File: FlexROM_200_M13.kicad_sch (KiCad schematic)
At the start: 9 parts, among them J1 HN61364_TANDY_200_M13, U1 FM16W08, U2 74LVC2G00

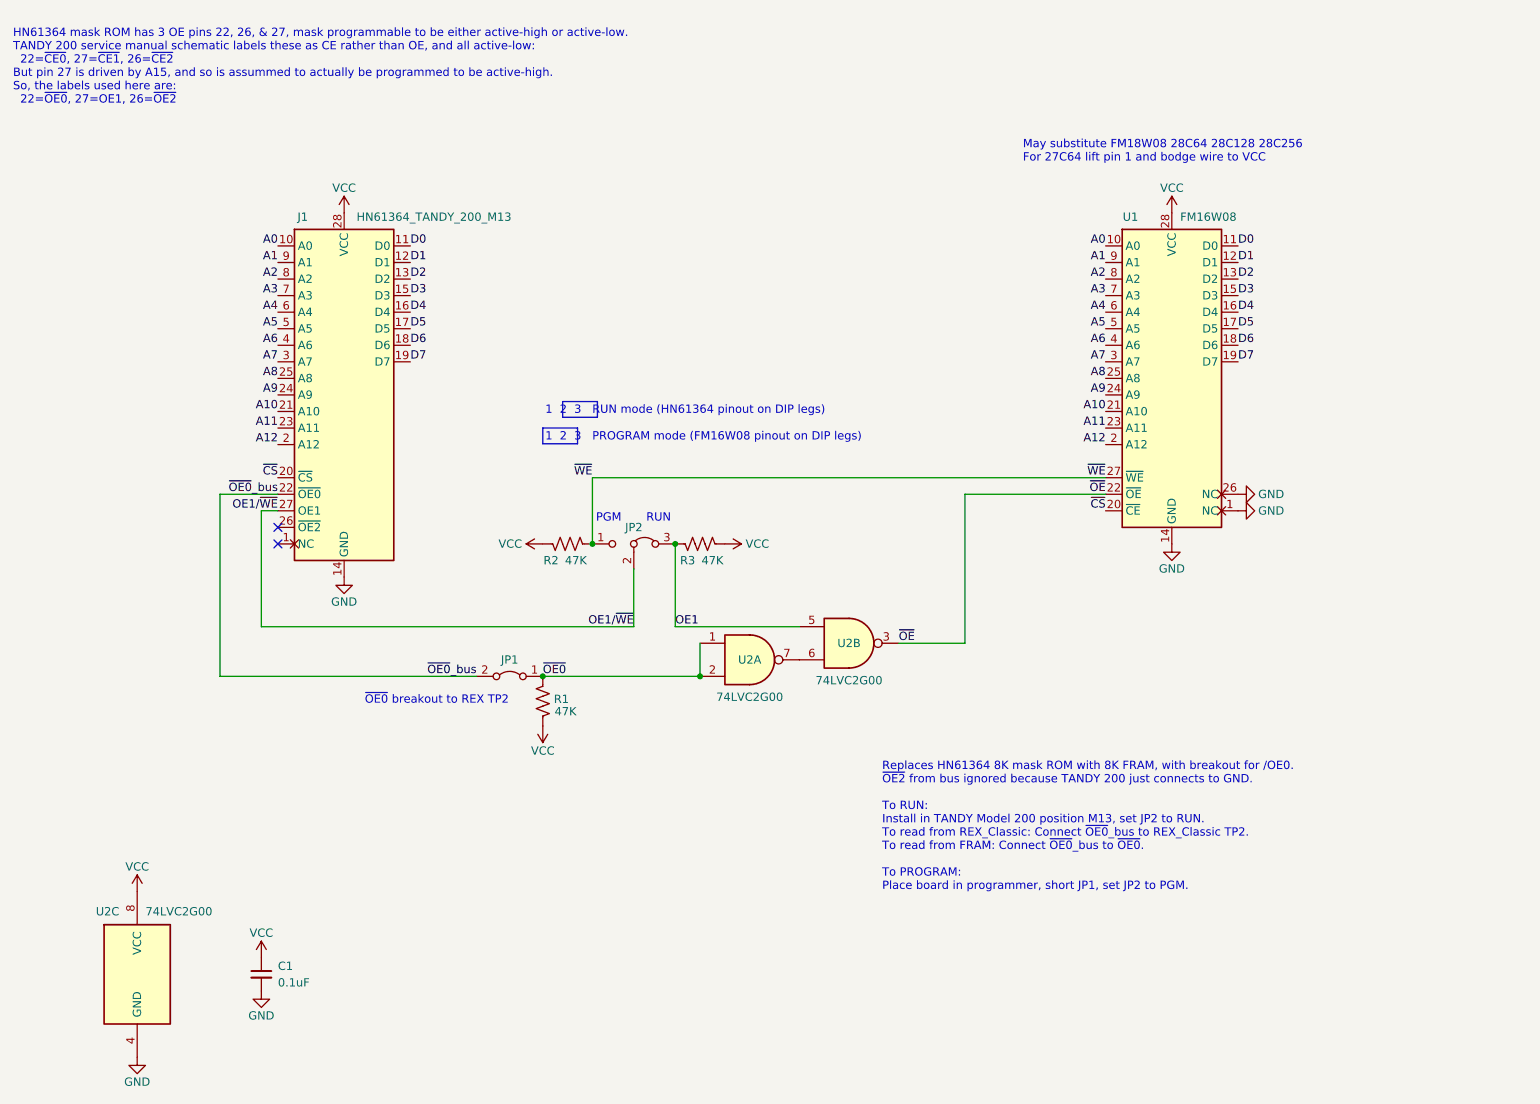
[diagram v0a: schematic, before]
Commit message: flexrom 102 & 200 accept eeprom or fram
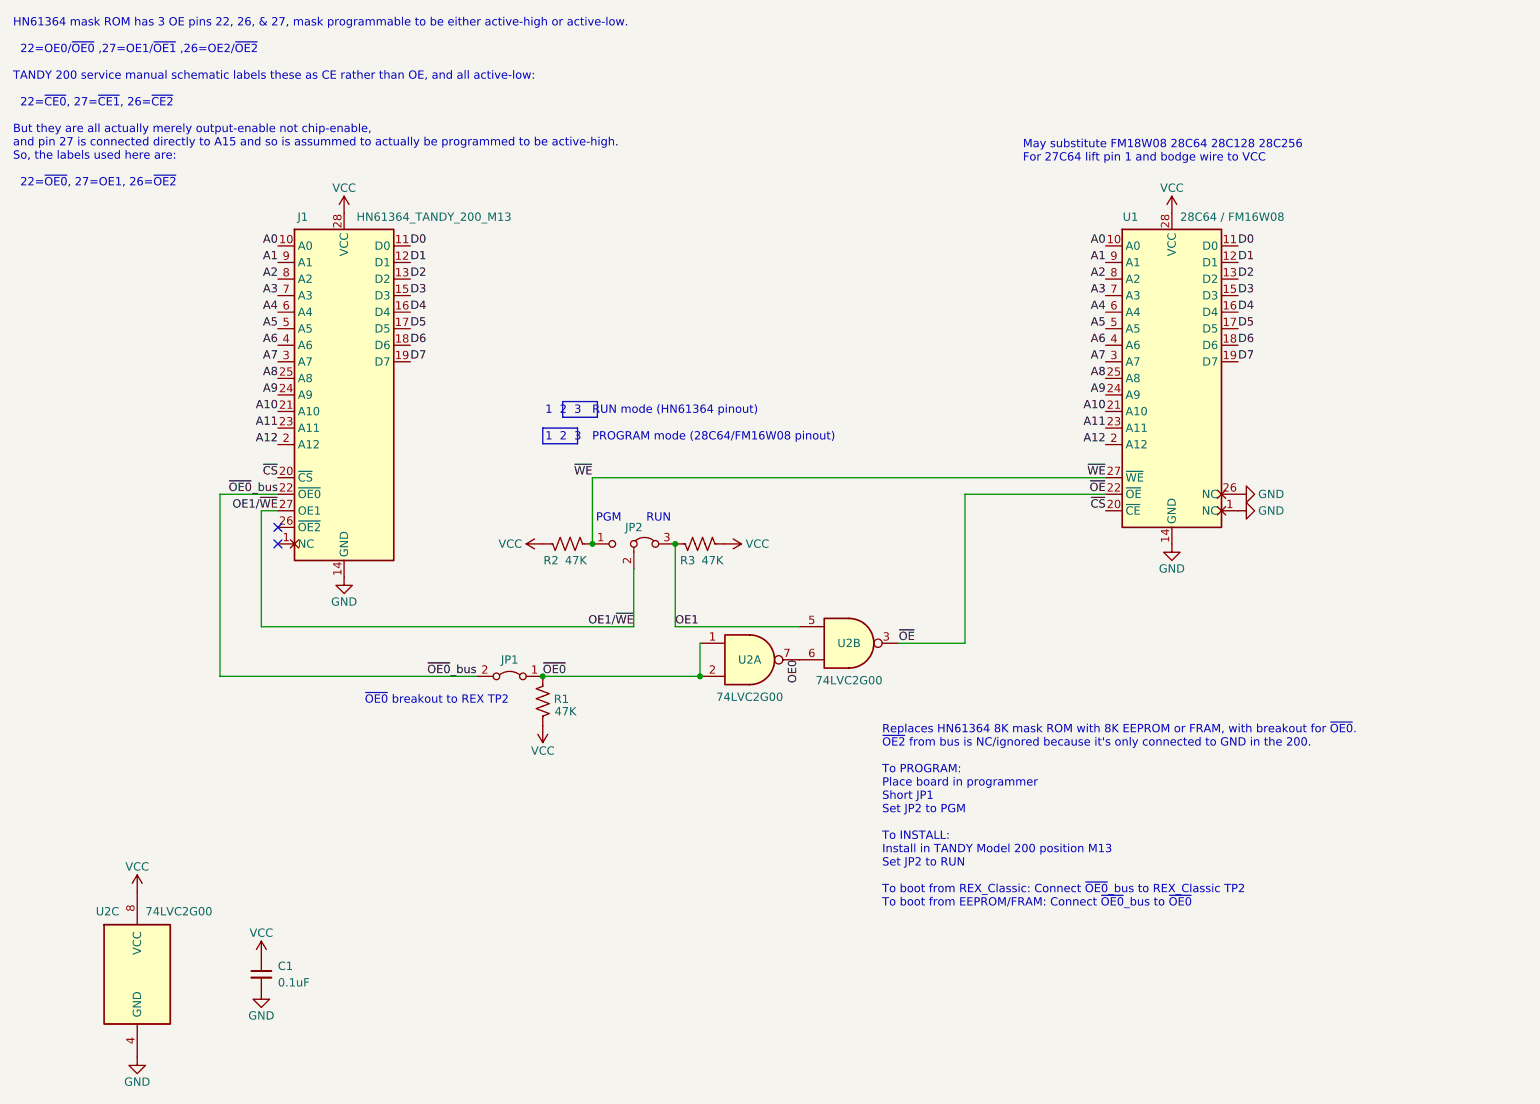
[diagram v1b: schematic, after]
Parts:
- U1: value FM16W08 -> 28C64 / FM16W08
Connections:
- net OE0: now reaches U2.6, U2.7
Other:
- note added: "1 2 3 RUN mode (HN61364 pinout) 1 2 3 PROGRAM mode (28C64/FM16W08 pinout)"
- note added: "HN61364 mask ROM has 3 OE pins 22, 26, & 27, mask programmable to be either active-high or active-low. 22=OE0/~{OE0} ,27=OE1/~{OE1} ,26=OE2/~{OE2} TANDY 200 service manual schematic labels these as CE rather than OE, and all active-low: 22=~{CE0}, 27=~{CE1}, 26=~{CE2} But they are all actually merely output-enable not chip-enable, and pin 27 is connected directly to A15 and so is assummed to actu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"
- note added: "Replaces HN61364 8K mask ROM with 8K EEPROM or FRAM, with breakout for ~{OE0}. ~{OE2} from bus is NC/ignored because it's only connected to GND in the 200. To PROGRAM: Place board in programmer Short JP1 Set JP2 to PGM To INSTALL: Install in TANDY Model 200 position M13 Set JP2 to RUN To boot from REX_Classic: Connect ~{OE0}_bus to REX_Classic TP2 To boot from EEPROM/FRAM: Connect ~{OE0}_bus to ~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"
- note removed: "1 2 3 RUN mode (HN61364 pinout on DIP legs) 1 2 3 PROGRAM mode (FM16W08 pinout on DIP legs)"
- note removed: "HN61364 mask ROM has 3 OE pins 22, 26, & 27, mask programmable to be either active-high or active-low. TANDY 200 service manual schematic labels these as CE rather than OE, and all active-low: 22=~{CE0}, 27=~{CE1}, 26=~{CE2} But pin 27 is driven by A15, and so is assummed to actually be programmed to be active-high. So, the labels used here are: 22=~{OE0}, 27=OE1, 26=~{OE2}"
- note removed: "Replaces HN61364 8K mask ROM with 8K FRAM, with breakout for /OE0. ~{OE2} from bus ignored because TANDY 200 just connects to GND. To RUN: Install in TANDY Model 200 position M13, set JP2 to RUN. To read from REX_Classic: Connect ~{OE0}_bus to REX_Classic TP2. To read from FRAM: Connect ~{OE0}_bus to ~{OE0}. To PROGRAM: Place board in programmer, short JP1, set JP2 to PGM."
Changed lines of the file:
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@@
     (stroke (width 0) (type solid) (color 0 0 0 0))
   )
-  (text "HN61364 mask ROM has 3 OE pins 22, 26, & 27, mask programmable to be either active-high or active-low.\nTANDY 200 service manual schematic labels these as CE rather than OE, and all active-low:\n  22=~{CE0}, 27=~{CE1}, 26=~{CE2}\nBut pin 27 is driven by A15, and so is assummed to actually be programmed to be active-high.\nSo, the labels used here are:\n  22=~{OE0}, 27=OE1, 26=~{OE2}\n"
-    (at 31.75 44.45 0)
-    (effects (font (size 1.27 1.27)) (justify left bottom))
-  )
-  (text "Replaces HN61364 8K mask ROM with 8K FRAM, with breakout for /OE0.\n~{OE2} from bus ignored because TANDY 200 just connects to GND.\n\nTo RUN:\nInstall in TANDY Model 200 position M13, set JP2 to RUN.\nTo read from REX_Classic: Connect ~{OE0}_bus to REX_Classic TP2.\nTo read from FRAM: Connect ~{OE0}_bus to ~{OE0}.\n\nTo PROGRAM:\nPlace board in programmer, short JP1, set JP2 to PGM.\n"
-    (at 165.1 165.1 0)
+  (text "HN61364 mask ROM has 3 OE pins 22, 26, & 27, mask programmable to be either active-high or active-low.\n\n  22=OE0/~{OE0} ,27=OE1/~{OE1} ,26=OE2/~{OE2}\n\nTANDY 200 service manual schematic labels these as CE rather than OE, and all active-low:\n\n  22=~{CE0}, 27=~{CE1}, 26=~{CE2}\n\nBut they are all actually merely output-enable not chip-enable,\nand pin 27 is connected directly to A15 and so is assummed to actually be programmed to be active-high.\nSo, the labels used here are:\n\n  22=~{OE0}, 27=OE1, 26=~{OE2}\n"
+    (at 31.75 57.15 0)
+    (effects (font (size 1.27 1.27)) (justify left bottom))
+  )
+  (text "Replaces HN61364 8K mask ROM with 8K EEPROM or FRAM, with breakout for ~{OE0}.\n~{OE2} from bus is NC/ignored because it's only connected to GND in the 200.\n\nTo PROGRAM:\nPlace board in programmer\nShort JP1\nSet JP2 to PGM\n\nTo INSTALL:\nInstall in TANDY Model 200 position M13\nSet JP2 to RUN\n\nTo boot from REX_Classic: Connect ~{OE0}_bus to REX_Classic TP2\nTo boot from EEPROM/FRAM: Connect ~{OE0}_bus to ~{OE0}"
+    (at 165.1 167.64 0)
     (effects (font (size 1.27 1.27)) (justify left bottom))
   )
@@
     (effects (font (size 1.27 1.27)) (justify left bottom))
   )
-  (text "1  2  3   RUN mode (HN61364 pinout on DIP legs)\n\n1  2  3   PROGRAM mode (FM16W08 pinout on DIP legs)"
+  (text "1  2  3   RUN mode (HN61364 pinout)\n\n1  2  3   PROGRAM mode (28C64/FM16W08 pinout)"
     (at 113.411 96.139 0)
     (effects (font (size 1.27 1.27)) (justify left bottom))
@@
     (effects (font (size 1.27 1.27)) (justify left bottom))
   )
+  (label "OE0" (at 152.4 129.54 270)
+    (effects (font (size 1.27 1.27)) (justify right bottom))
+  )
   (label "A7" (at 199.39 83.82 180)
     (effects (font (size 1.27 1.27)) (justify right bottom))
@@
     (in_bom yes) (on_board yes)
     (property "Reference" "U1" (id 0) (at 203.2 61.595 0))
-    (property "Value" "FM16W08" (id 1) (at 210.82 61.595 0)
+    (property "Value" "28C64 / FM16W08" (id 1) (at 210.82 61.595 0)
       (effects (font (size 1.27 1.27)) (justify left))
     )
@@
     )
     (path "/00000000-0000-0000-0000-00005e5b130a"
-      (reference "U1") (unit 1) (value "FM16W08") (footprint "000_LOCAL:SOIC28W")
+      (reference "U1") (unit 1) (value "28C64 / FM16W08") (footprint "000_LOCAL:SOIC28W")
     )
     (path "/5c32c56a-9bae-4a48-bfd8-3977d42bd228"
